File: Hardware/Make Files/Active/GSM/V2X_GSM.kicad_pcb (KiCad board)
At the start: 2 copper layers, 85 x 56 mm, 50 parts, among them P1 47553-1001, P11 Ficudial2, P13 Ficudial3, P16 Ficudial4, P18 CUR_SEN, P2 SMA, P26 CONN_02X08, P3 SMA, P7 Ficudial1, Q12 IRF9335, U14 XRP6124, U3 MMQA5V6T3G, U4 SIM5320

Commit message: V2X V1.2 PCB build, with shares
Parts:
- moved R9 21.0 mm to (152.0, 127.0)
- moved R8 1.50 mm to (152.0, 129.5)
- moved R84 0.50 mm to (152.0, 124.5)
- moved R85 0.50 mm to (152.0, 122.0)
- renumbered C47 to C46, C46 to C47, D13 to D3, P18 to P14, R63 to R16, R64 to R17, U14 to U13
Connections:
- P26 pad 2: GND -> SIM_WAKE_B
- U4 pad 15: (no net) -> Net-(U4-Pad15)
- U4 pad 16: (no net) -> Net-(U4-Pad16)
- U4 pad 21: (no net) -> Net-(U4-Pad21)
- U4 pad 22: (no net) -> Net-(U4-Pad22)
- U4 pad 23: (no net) -> Net-(U4-Pad23)
- U4 pad 24: (no net) -> Net-(U4-Pad24)
- U4 pad 25: (no net) -> Net-(U4-Pad25)
- U4 pad 26: (no net) -> Net-(U4-Pad26)
- U4 pad 27: (no net) -> Net-(U4-Pad27)
- U4 pad 28: (no net) -> Net-(U4-Pad28)
- U4 pad 29: (no net) -> Net-(U4-Pad29)
- U4 pad 30: (no net) -> Net-(U4-Pad30)
- U4 pad 31: (no net) -> Net-(U4-Pad31)
- U4 pad 32: (no net) -> Net-(U4-Pad32)
- U4 pad 33: (no net) -> Net-(U4-Pad33)
- U4 pad 34: (no net) -> Net-(U4-Pad34)
- U4 pad 35: (no net) -> Net-(U4-Pad35)
- U4 pad 36: (no net) -> Net-(U4-Pad36)
- U4 pad 44: (no net) -> Net-(U4-Pad44)
- U4 pad 45: (no net) -> Net-(U4-Pad45)
- U4 pad 46: (no net) -> Net-(U4-Pad46)
- U4 pad 47: (no net) -> Net-(U4-Pad47)
- U4 pad 48: (no net) -> Net-(U4-Pad48)
- U4 pad 50: (no net) -> SIM_WAKE_B
- U4 pad 53: (no net) -> Net-(U4-Pad53)
- U4 pad 55: (no net) -> Net-(U4-Pad55)
- U4 pad 56: (no net) -> Net-(U4-Pad56)
- U4 pad 6: (no net) -> Net-(U4-Pad6)
- U4 pad 66: (no net) -> Net-(U4-Pad66)
- U4 pad 67: (no net) -> Net-(U4-Pad67)
- U4 pad 7: (no net) -> Net-(U4-Pad7)
- U4 pad 70: (no net) -> Net-(U4-Pad70)
- U4 pad 73: (no net) -> Net-(U4-Pad73)
- U4 pad 74: (no net) -> Net-(U4-Pad74)
- U4 pad 75: (no net) -> Net-(U4-Pad75)
- U4 pad 76: (no net) -> Net-(U4-Pad76)
- U4 pad 8: (no net) -> Net-(U4-Pad8)
- U4 pad 9: (no net) -> Net-(U4-Pad9)
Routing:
- net GND: track 839.4 -> 868.1 mm, vias 194 -> 199
- net SIM_WAKE_B: track 0.00 -> 20.4 mm, vias 0 -> 3
- net 12V0_C: track 12.4 -> 0.00 mm, vias 7 -> 0
- net SIMCARD_B: track 57.5 -> 67.7 mm
- net 4V1_EN_B: track 27.7 -> 21.8 mm
- net SIM_RF_OFF_B: track 23.0 -> 25.6 mm, vias 2 -> 1
- net 4V1_B: track 59.3 -> 56.9 mm, vias 2 -> 3
- net SIM_RI: track 46.0 -> 47.3 mm, vias 4 -> 2
- net SIM_PWR_ON_B: track 53.6 -> 54.7 mm
- net SIM_RXD_B: track 60.5 -> 61.6 mm, vias 1 -> 2
- net SIM_TXD_B: track 60.6 -> 61.6 mm, vias 2 -> 1
- net SIM_PWR_B: track 24.5 -> 25.2 mm
- removed copper zone on B.Cu, net 12V0_C
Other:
- board text added: "GSM+GPS BOARD JAGUAR LAND ROVER OSTC RVI V2X V1.2"
- board text added: "Jesse Banks 2015"
- board text removed: "JAGUAR LAND ROVER OSTC RVI V2X V1.2 2015 M2M+GPS BOARD"
- board text removed: "Jesse Banks"

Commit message: V1.2 Ordered
This is a capture of the project folder at the time f ordering the V1.2
kit.
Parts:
- removed C22: 47p, Custom Parts:C_0603_SM
- removed L6, L7: 47N, Custom Parts:C_0603_SM
- removed P11: Ficudial2, Fiducials:Fiducial_1mm_Dia_2.54mm_Outer_CopperTop
- removed P13: Ficudial3, Fiducials:Fiducial_1mm_Dia_2.54mm_Outer_CopperTop
- removed P16: Ficudial4, Fiducials:Fiducial_1mm_Dia_2.54mm_Outer_CopperTop
- removed P7: Ficudial1, Fiducials:Fiducial_1mm_Dia_2.54mm_Outer_CopperTop
- added U24: TLV70012DCK, Housings_SOT-23_SOT-143_TSOT-6:SOT-23-5, F.Cu at (177.5, 97.5)
- C17: value 330P -> 56P
- C18: value 10N -> 470P
- C19: value 330P -> 100N
- C20: value 10N -> 4U7; footprint Custom Parts:C_0603_SM -> Custom Parts:C_0805_SM
- C21: value 47p -> 150p
- L1: value 47N -> 330N
- L2: value 47N -> 120N
- P1: value 47553-1001 -> SIM_SKT
- P26: value CONN_02X08 -> CONN_02X10
- moved U3 58.6 mm to (129.5, 87.0), turned to 270 degrees
- moved R12 48.1 mm to (124.5, 92.0), turned to 90 degrees
- moved R14 44.4 mm to (127.5, 92.0), turned to 90 degrees
- moved R13 40.7 mm to (130.5, 92.0), turned to 90 degrees
- moved C19 32.1 mm to (173.5, 97.5)
- moved C20 27.9 mm to (181.5, 97.5), turned to 270 degrees
- moved C27 8.42 mm to (168.0, 108.0), turned to 90 degrees
- moved C28 6.12 mm to (168.0, 113.0), turned to 270 degrees
- moved L1 3.71 mm to (185.1, 93.1), turned to 0 degrees
- moved C21 3.50 mm to (187.0, 88.5)
- moved C18 2.85 mm to (188.5, 94.0)
- moved C14 2.63 mm to (168.0, 99.0), turned to 270 degrees
- moved C17 2.02 mm to (191.0, 94.0), turned to 270 degrees
- moved L2 1.00 mm to (191.0, 89.5)
- moved C15 0.64 mm to (168.0, 103.5), turned to 90 degrees
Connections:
- C17 pad 1: GND -> Net-(C17-Pad1)
- C17 pad 2: Net-(C17-Pad2) -> GND
- C18 pad 1: Net-(C17-Pad2) -> Net-(C17-Pad1)
- C19 pad 1: GND -> 4V1F1
- C19 pad 2: Net-(C19-Pad2) -> GND
- C20 pad 1: Net-(C19-Pad2) -> 3V3F1
- L1 pad 1: 4V1F1 -> 3V3F1
- L1 pad 2: Net-(C17-Pad2) -> Net-(C17-Pad1)
- L2 pad 2: Net-(C17-Pad2) -> Net-(C17-Pad1)
- P1 pad : (no net) -> GND
- P3 pad 1: GSM -> GSM_ANT
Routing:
- net GND: track 868.1 -> 1002.7 mm, vias 199 -> 356
- net SIMCARD_DATA: track 18.1 -> 86.7 mm, vias 0 -> 2
- net SIMCARD_CLK: track 17.0 -> 81.8 mm, vias 0 -> 2
- net SIMCARD_RESET: track 20.4 -> 72.9 mm, vias 0 -> 2
- net Net-(R14-Pad1): track 51.7 -> 17.1 mm, vias 2 -> 0
- net 4V1F1: track 26.9 -> 61.1 mm, vias 2 -> 6
- net Net-(R13-Pad1): track 48.2 -> 15.1 mm, vias 2 -> 0
- net Net-(R12-Pad1): track 50.0 -> 22.7 mm, vias 2 -> 0
- net SIMCARD_B: track 67.7 -> 89.6 mm
- net Net-(C17-Pad2): track 15.7 -> 0.00 mm
- net GSM: track 14.4 -> 0.00 mm
- net Net-(C19-Pad2): track 12.9 -> 0.00 mm
- net GSM_ANT: track 32.5 -> 44.0 mm
- net GPS: track 17.1 -> 8.20 mm
- net Net-(C17-Pad1): track 0.00 -> 7.90 mm
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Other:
- net class RF: trace_width 1.05 -> 1.08
- net class USB added: clearance 0.2, trace_width 0.22, via_dia 0.6, via_drill 0.4

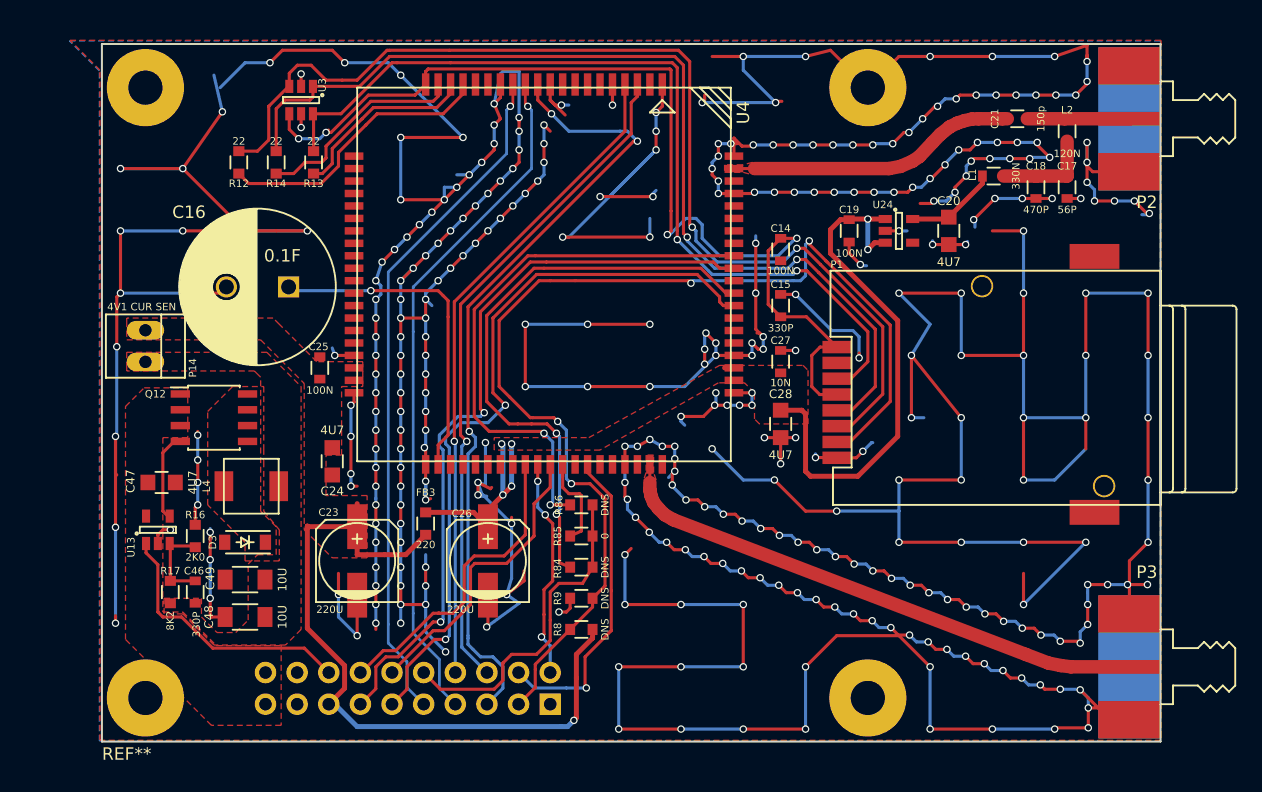
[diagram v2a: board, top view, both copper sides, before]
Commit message: GSM board update
new FPC connector, sim5320 moved towards rf connectors
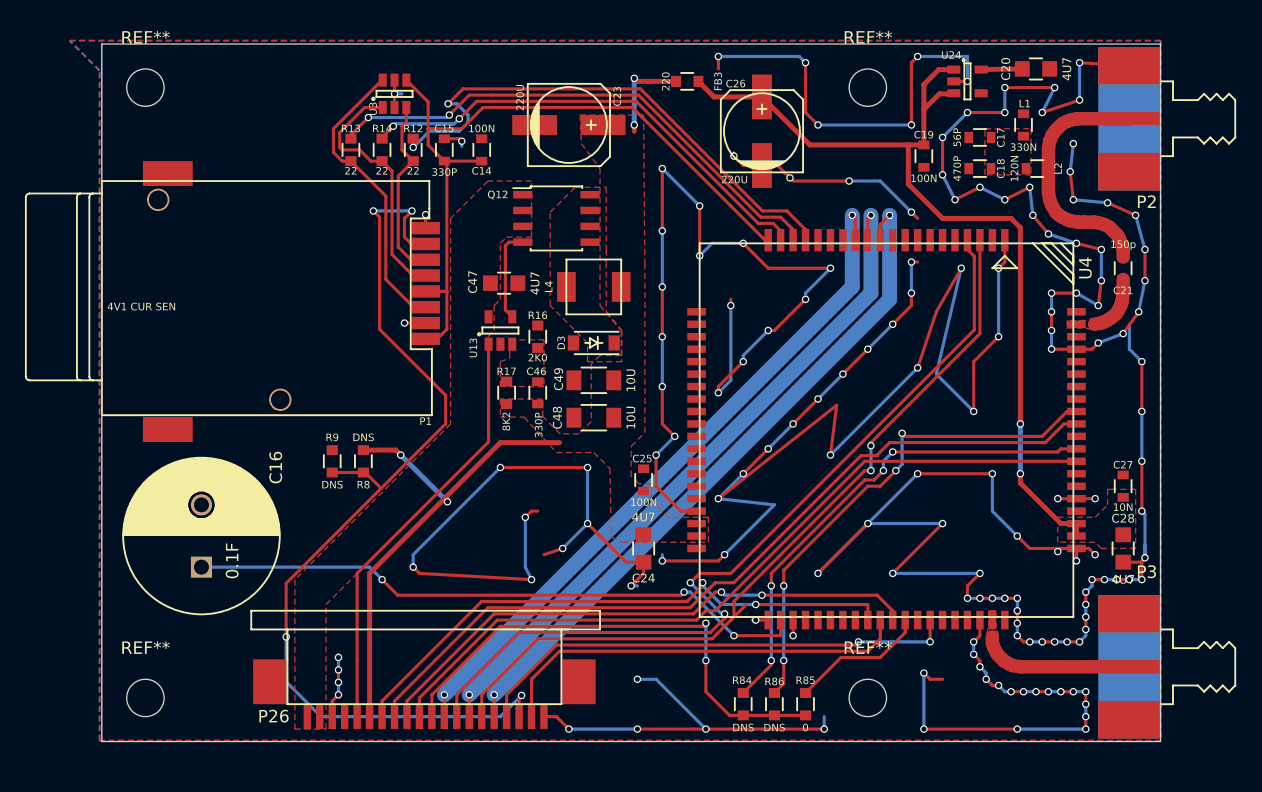
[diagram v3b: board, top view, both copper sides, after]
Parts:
- removed P14: CUR_SEN, Connect:PINHEAD1-2
- removed the REF** at (117.0, 135.0)
- added REF**: MountingHole_3mm, Mounting_Holes:MountingHole_3mm, F.Cu at (117.0, 135.0)
- added REF**: MountingHole_3mm, Mounting_Holes:MountingHole_3mm, F.Cu at (175.0, 135.0)
- added REF**: MountingHole_3mm, Mounting_Holes:MountingHole_3mm, F.Cu at (175.0, 86.0)
- added REF**: MountingHole_3mm, Mounting_Holes:MountingHole_3mm, F.Cu at (117.0, 86.0)
- P26: footprint Pin_Headers:Pin_Header_Straight_2x10 -> Custom Parts:FFC-1MMx20; moved to F.Cu
- moved P1 60.4 mm to (126.0, 103.0), turned to 180 degrees
- moved FB3 41.2 mm to (160.5, 85.5), turned to 180 degrees
- moved C26 40.9 mm to (166.5, 89.5)
- moved C23 38.9 mm to (151.0, 89.0), turned to 0 degrees
- moved C48 32.2 mm to (153.0, 112.5)
- moved C49 32.2 mm to (153.0, 109.5)
- moved D3 32.2 mm to (153.0, 106.5)
- moved C47 31.8 mm to (145.8, 101.7)
- moved C46 31.8 mm to (148.5, 110.5)
- moved L4 31.8 mm to (153.0, 102.0)
- moved Q12 31.8 mm to (150.0, 96.5)
- moved R16 31.8 mm to (148.5, 106.0)
- moved U13 31.8 mm to (145.5, 105.5)
- moved R17 31.4 mm to (146.0, 110.5)
- moved U4 30.2 mm to (176.5, 113.5)
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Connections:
- C46 pad 1: Net-(C46-Pad1) -> 4V1_B
- C48 pad 1: Net-(C46-Pad1) -> 4V1_B
- C49 pad 1: Net-(C46-Pad1) -> 4V1_B
- L4 pad 2: Net-(C46-Pad1) -> 4V1_B
- P1 pad : GND -> (no net)
- R17 pad 1: Net-(C46-Pad1) -> 4V1_B
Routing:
- net GND: track 1002.7 -> 552.8 mm, vias 356 -> 159
- net SIMCARD_DATA: track 86.7 -> 14.8 mm, vias 2 -> 0
- net SIMCARD_CLK: track 81.8 -> 20.6 mm, vias 2 -> 0
- net SIMCARD_RESET: track 72.9 -> 23.9 mm, vias 2 -> 0
- net GSM_ANT: track 44.0 -> 12.4 mm
- net Net-(R13-Pad1): track 15.1 -> 42.4 mm, vias 0 -> 2
- net Net-(C16-Pad1): track 27.1 -> 50.2 mm, vias 1 -> 3
- net SIMCARD_V: track 83.2 -> 60.7 mm, vias 4 -> 0
- net Net-(R14-Pad1): track 17.1 -> 38.4 mm, vias 0 -> 2
- net SIM_PWR_B: track 25.4 -> 46.5 mm, vias 0 -> 2
- net Net-(R12-Pad1): track 22.7 -> 43.2 mm, vias 0 -> 2
- net SIM_NET_B: track 24.9 -> 45.2 mm, vias 0 -> 2
- net GPS_ANT: track 23.3 -> 4.84 mm
- net SIM_WAKE_B: track 17.9 -> 33.8 mm, vias 3 -> 0
- net SIM_RESET_B: track 52.9 -> 68.6 mm, vias 1 -> 2
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- added copper zone on F.Cu, net Net-(C17-Pad1)
- added copper zone on F.Cu, net Net-(C46-Pad2)
- removed copper zone on F.Cu, net Net-(C46-Pad1)
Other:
- net class USB: clearance 0.2 -> 0.16; trace_width 0.22 -> 1.2

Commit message: small changes to GSM layout
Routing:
- net 3V3F1: track 3.30 -> 6.94 mm
- net SIM_PWR_ON_B: track 65.1 -> 63.3 mm
- net GND: track 552.8 -> 552.1 mm
- net Net-(P26-Pad10): track 40.4 -> 39.8 mm
